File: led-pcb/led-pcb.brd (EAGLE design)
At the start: 24 x 40 mm, 9 parts, among them U1 RFD22102, U2 IC REG LDO 3.3V

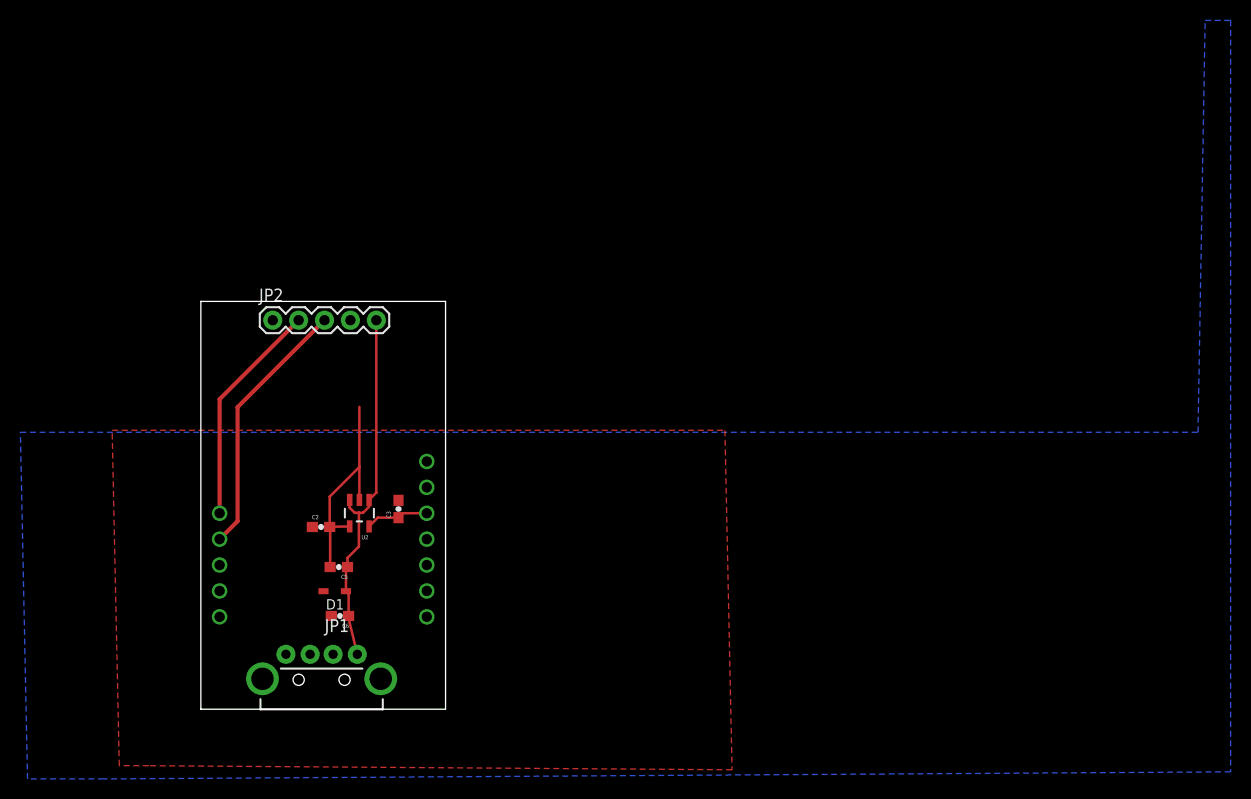
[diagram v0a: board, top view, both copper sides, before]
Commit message: circle pcb, and updated usb pcb
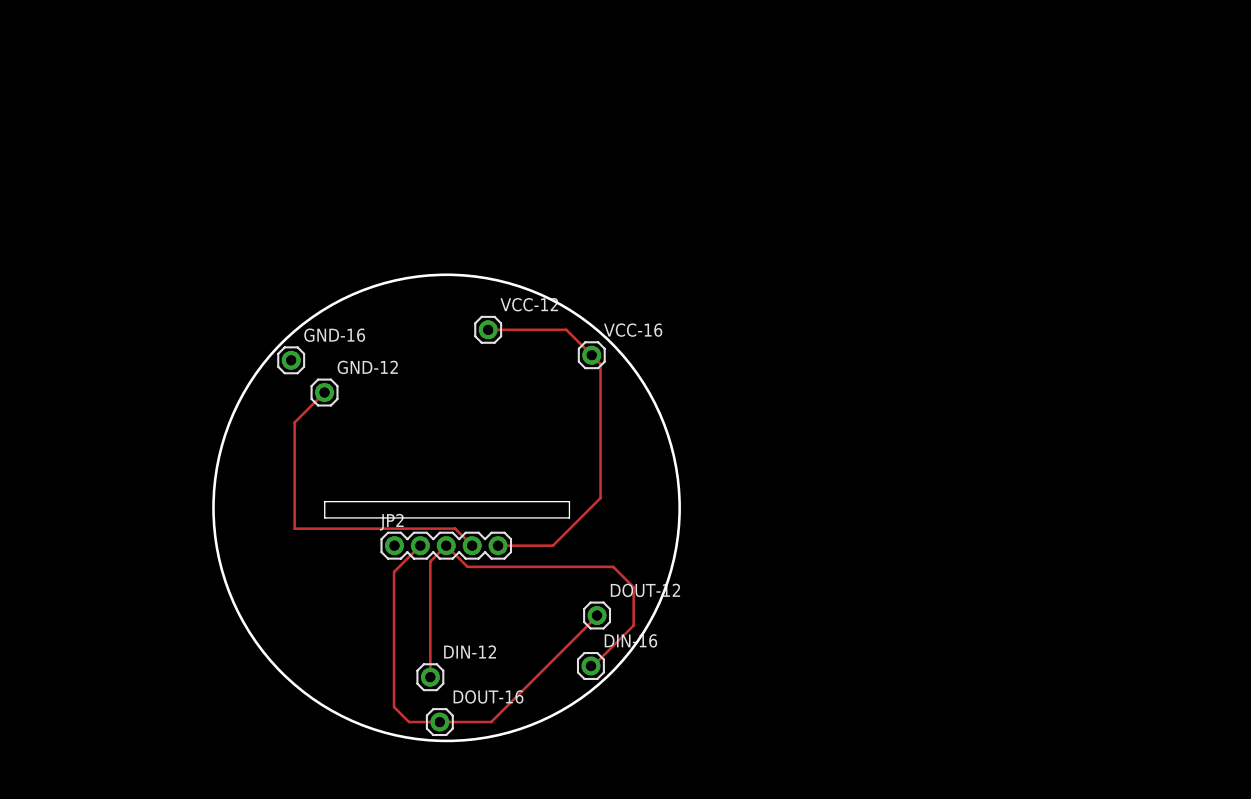
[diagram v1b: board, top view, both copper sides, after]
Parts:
- removed C2: 470pF, SparkFun-Capacitors:0603-CAP
- removed C3: 2.2uF, SparkFun-Capacitors:0603-CAP
- removed C5: 4.7uF, SparkFun-Capacitors:0603-CAP
- removed C6: 10nF, SparkFun-Capacitors:0603-CAP
- removed D1: TVS Diode 5VWM 9.8VDC SOD323, zetex:SOD323
- removed JP1: USB-A-H, SparkFun-Connectors:USB-A-H
- removed U1: RFD22102, RF_Digital_RFD22102_Eagle_Schematic_PCB_Library:RFD22102
- removed U2: IC REG LDO 3.3V, SparkFun-PowerIC:SOT23-5
- added DIN-12, DIN-16, DOUT-12, DOUT-16, GND-12, GND-16, VCC-12, VCC-16: M01PTH, USB3.0:1X01
- JP2: device SparkFun-Connectors:1X05 -> USB3.0:1X05
- moved JP2 25.1 mm to (20.3, 30.6)
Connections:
- removed net 3.3V: C3.1, U1.VCC, U2.5
- removed net N$2: C2.1, U2.4
- removed net VBUS: C5.1, C6.1, D1.1, JP1.VBUS, JP2.5, U2.1, U2.3
- new net VCC: JP2.5, VCC-12.1, VCC-16.1
- net DIN: now also DIN-12.1, DIN-16.1; no longer U1.GPIO5
- net DOUT: now also DOUT-12.1, DOUT-16.1; no longer U1.GPIO6
- net GND: now also GND-12.1, GND-16.1; no longer C2.2, C3.2, C5.2, C6.2, D1.2, JP1.GND, U1.GND, U2.2
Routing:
- net VCC: track 0.00 -> 37.5 mm
- net VBUS: track 36.3 -> 0.00 mm
- net DOUT: track 22.1 -> 41.9 mm
- net DIN: track 25.7 -> 43.2 mm
- net GND: track 20.2 -> 32.7 mm
- net 3.3V: track 6.20 -> 0.00 mm
- net N$2: track 3.66 -> 0.00 mm
- removed copper zone on layer 1, net GND
- removed copper zone on layer 16, net GND
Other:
- board size 24 x 40 mm -> 45.7 x 45.7 mm
